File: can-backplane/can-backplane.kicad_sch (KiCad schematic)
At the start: 51 parts, among them J1 BATT, J10 DSUB-9, J11 DSUB-9, J12 Raspberry_Pi, J13 DSUB-9, J14 DSUB-9, J15 DSUB-9, J16 DSUB-9, J17 DSUB-9, J18 DSUB-9, J19 DSUB-9, J2 DSUB-9, J20 DSUB-9, J21 DSUB-9, J22 DSUB-9, J3 DSUB-9, J4 DSUB-9, J5 DSUB-9, J6 DSUB-9, J7 DSUB-9, J8 DSUB-9, J9 DSUB-9, U1 TPS566242DRLR, U2 TCAN1044VDDFR, U3 MCP2517FD-xJHA, Y1 40MHz

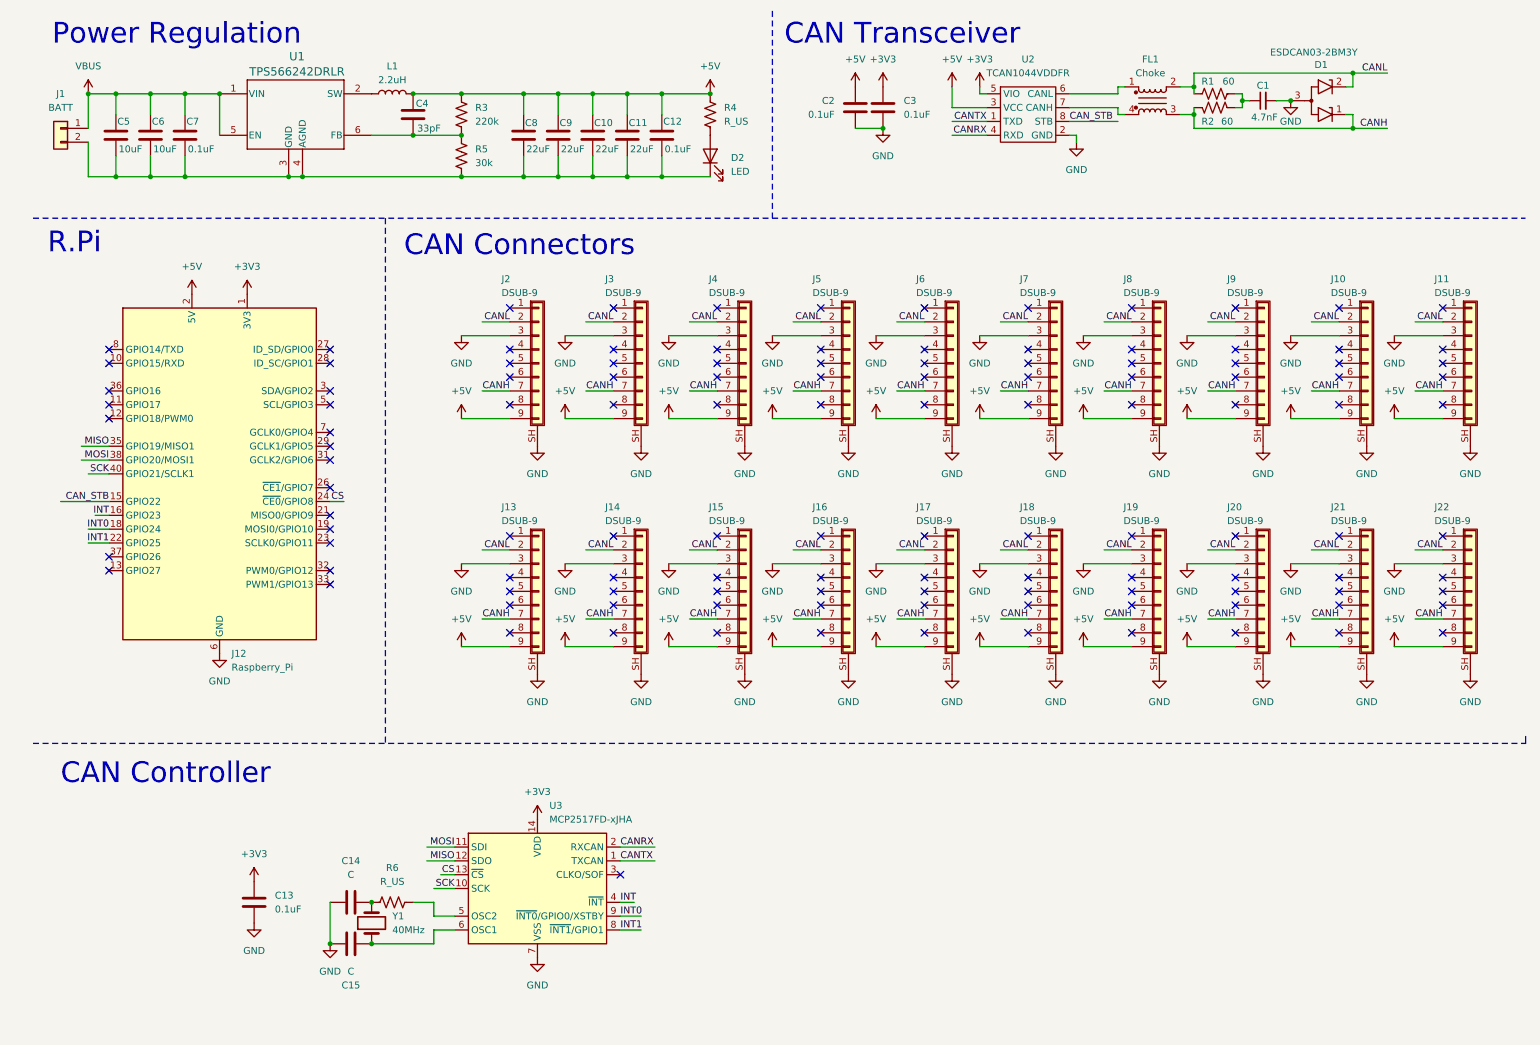
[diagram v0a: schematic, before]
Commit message: Added serial
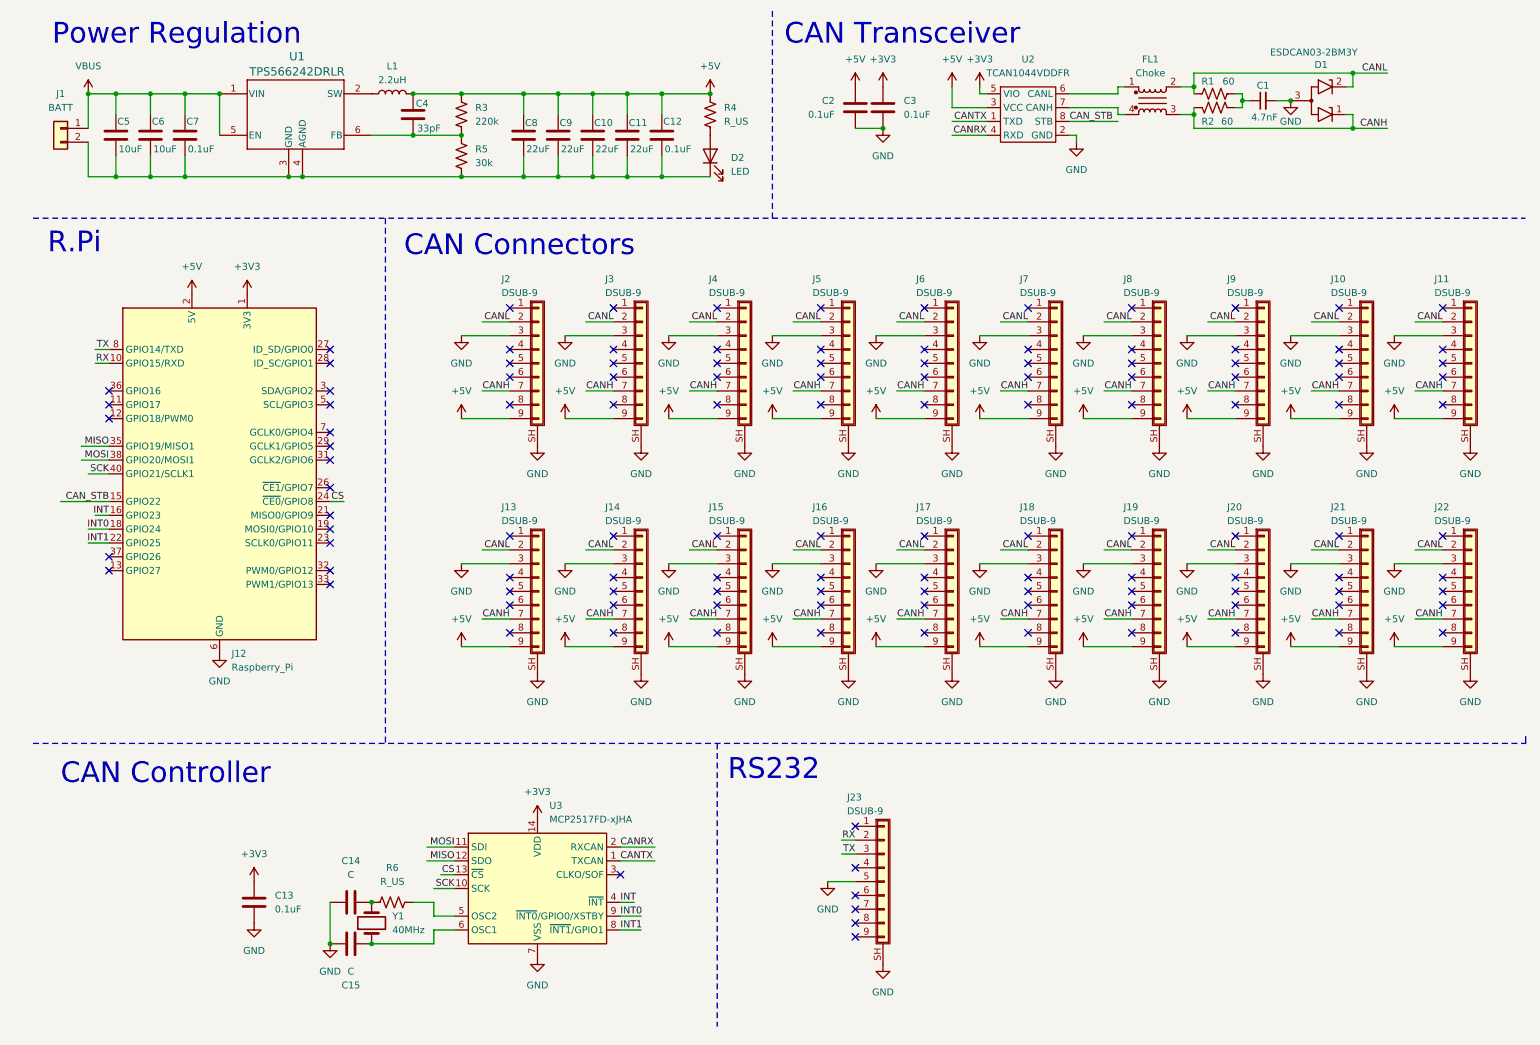
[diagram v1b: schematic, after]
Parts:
- added J23: DSUB-9, symbol Connector_Generic_Shielded:Conn_01x09_Shielded
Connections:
- net GND: now also J23.5 (Pin_5), J23.SH (Shield)
- net RX: now reaches J12.10 (GPIO15/RXD)
- net RX: now also J23.2 (Pin_2)
- net TX: now reaches J12.8 (GPIO14/TXD)
- net TX: now also J23.3 (Pin_3)
- no-connect marks 121 -> 125
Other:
- note added: "RS232"

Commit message: Added level shifting
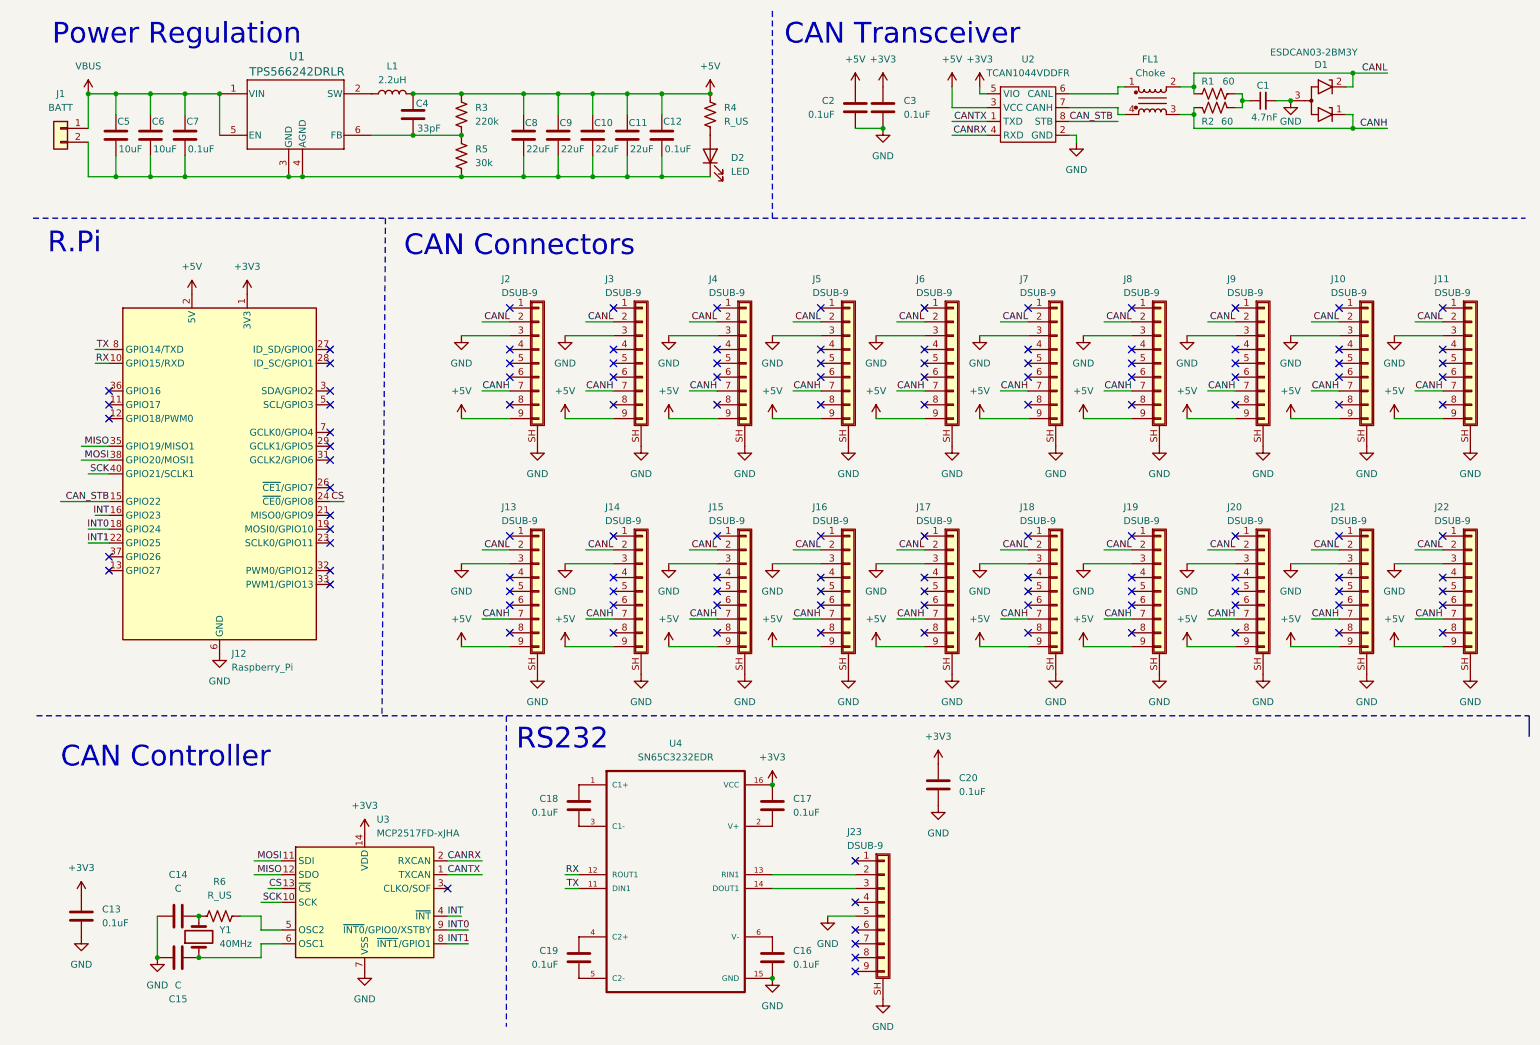
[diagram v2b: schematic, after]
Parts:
- added C16, C17, C18, C19, C20: 0.1uF, symbol Device:C
- added U4: SN65C3232EDR, SN65C3232EDR:SOIC127P600X175-16N, symbol Railspeeder:SN65C3232EDR
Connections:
- net +3V3: now also C17.1, C20.1, U4.16 (VCC)
- net GND: now also C16.2, C20.2, U4.15 (GND)
- net RX: now also U4.12 (ROUT1); no longer J23.2 (Pin_2)
- net TX: now also U4.11 (DIN1); no longer J23.3 (Pin_3)
- new net: C18.1, U4.1 (C1+)
- new net: C18.2, U4.3 (C1-)
- new net: C19.1, U4.4 (C2+)
- new net: C19.2, U4.5 (C2-)
- new net: J23.2 (Pin_2), U4.13 (RIN1)
- new net: J23.3 (Pin_3), U4.14 (DOUT1)
- new net: C17.2, U4.2 (V+)
- new net: C16.1, U4.6 (V-)
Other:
- moved on the sheet: C13, C14, C15, J23, R6, U3, Y1

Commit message: Component selection
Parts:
- C10, C11, C12, C16, C17, C18, C19, C20, C4, C5, C6, C7, C8, C9: footprint (none) -> Capacitor_SMD:C_0603_1608Metric
- C14, C15: value C -> CL; footprint (none) -> Capacitor_SMD:C_0603_1608Metric
- D2: value LED -> GREEN; footprint (none) -> LED_SMD:LED_0603_1608Metric
- J1: footprint (none) -> Connector_PinSocket_2.54mm:PinSocket_1x02_P2.54mm_Vertical
- J10, J11, J13, J14, J15, J16, J17, J18, J19, J2, J20, J21, J22, J23, J3, J4, J5, J6, J7, J8, J9: footprint (none) -> Connector_Dsub:DSUB-9_Female_Vertical_P2.77x2.84mm_MountingHoles
- J12: footprint (none) -> railspeeder:RPI_Hat_B+
- L1: footprint (none) -> Inductor_SMD_Wurth:L_Wurth_WE-LQSH-4020
- R3, R5: footprint (none) -> Resistor_SMD:R_0603_1608Metric
- R4: value R_US -> 220; footprint (none) -> Resistor_SMD:R_0603_1608Metric
- R6: value R_US -> REXT; footprint (none) -> Resistor_SMD:R_0603_1608Metric
- U1: footprint SOT5x3_DRL_TEX -> railspeeder:SOT5x3_DRL_TEX
- U4: footprint SN65C3232EDR:SOIC127P600X175-16N -> Package_SO:SOIC-16_3.9x9.9mm_P1.27mm
- Y1: footprint (none) -> Crystal:Crystal_SMD_Abracon_ABM10-4Pin_2.5x2.0mm

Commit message: PCB Work
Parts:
- added C21, C22: 4.7nF, Capacitor_SMD:C_0603_1608Metric, symbol Device:C_Small
- added R7: 5.1k, Resistor_SMD:R_0603_1608Metric, symbol Device:R_US
- J1: footprint Connector_PinSocket_2.54mm:PinSocket_1x02_P2.54mm_Vertical -> TerminalBlock_WAGO:TerminalBlock_WAGO_236-102_1x02_P5.00mm_45Degree
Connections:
- net +3V3: now also R7.2; no longer C17.1
- net CANH: now also C21.2
- net CANL: now also C22.2
- net CAN_STB: now also R7.1
- net GND: now also C17.2, C21.1, C22.1
- net at U4.2 (V+): now also C17.1; no longer C17.2
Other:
- moved on the sheet: C1, C17, D1

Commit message: PCB Work
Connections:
- net CANH: now also D1.2 (K2); no longer D1.1 (K1)
- net CANL: now also D1.1 (K1); no longer D1.2 (K2)
- net GND: now also C10.2, C11.2, C12.2, C5.2, C6.2, C7.2, C8.2, C9.2, D2.1 (K), J1.2 (Pin_2), R5.2, U1.3 (GND), U1.4 (AGND)
- net INT0: now also J12.22 (GPIO25); no longer J12.18 (GPIO24)
- net INT1: now also J12.18 (GPIO24); no longer J12.22 (GPIO25)
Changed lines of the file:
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@@
 	)
 	(junction
-		(at 254 27.94)
+		(at 135.89 41.91)
 		(diameter 0)
 		(color 0 0 0 0)
@@
 	)
 	(junction
+		(at 254 27.94)
+		(diameter 0)
+		(color 0 0 0 0)
+	)
+	(junction
 		(at 33.02 41.91)
 		(diameter 0)
@@
 	)
 	(label "INT0"
-		(at 25.4 106.68 180)
+		(at 25.4 109.22 180)
 		(fields_autoplaced yes)
 		(effects
@@
 	)
 	(label "INT1"
-		(at 25.4 109.22 180)
+		(at 25.4 106.68 180)
 		(fields_autoplaced yes)
 		(effects
@@
 	(symbol
 		(lib_id "power:GND")
+		(at 135.89 41.91 0)
+		(unit 1)
+		(exclude_from_sim no)
+		(in_bom yes)
+		(on_board yes)
+		(dnp no)
+		(fields_autoplaced yes)
+		(property "Reference" "#PWR086"
+			(at 135.89 48.26 0)
+			(effects
+				(font
+					(size 1.27 1.27)
+				)
+				(hide yes)
+			)
+		)
+		(property "Value" "GND"
+			(at 135.89 46.99 0)
+			(effects
+				(font
+					(size 1.27 1.27)
+				)
+			)
+		)
+		(property "Footprint" ""
+			(at 135.89 41.91 0)
+			(effects
+				(font
+					(size 1.27 1.27)
+				)
+				(hide yes)
+			)
+		)
+		(property "Datasheet" ""
+			(at 135.89 41.91 0)
+			(effects
+				(font
+					(size 1.27 1.27)
+				)
+				(hide yes)
+			)
+		)
+		(property "Description" "Power symbol creates a global label with name \"GND\" , ground"
+			(at 135.89 41.91 0)
+			(effects
+				(font
+					(size 1.27 1.27)
+				)
+				(hide yes)
+			)
+		)
+		(pin "1"
+		)
+		(instances
+			(project "can-backplane"
+				(path "/6aa1e968-9fc5-4472-b994-95c9fa68b877"
+					(reference "#PWR086")
+					(unit 1)
+				)
+			)
+		)
+	)
+	(symbol
+		(lib_id "power:GND")
 		(at 104.14 133.35 0)
 		(unit 1)
@@
 		(lib_id "Power_Protection:RCLAMP0582B")
 		(at 259.08 27.94 0)
-		(mirror x)
 		(unit 1)
 		(exclude_from_sim no)
@@
 		(dnp no)
 		(property "Reference" "D1"
-			(at 259.588 21.336 0)
+			(at 259.588 34.544 0)
 			(effects
 				(font
@@
 		)
 		(property "Value" "ESDCAN03-2BM3Y"
-			(at 258.2545 19.05 0)
+			(at 258.2545 36.83 0)
 			(effects
 				(font
@@
 		)
 		(property "Footprint" "Package_TO_SOT_SMD:SOT-416"
-			(at 259.08 20.32 0)
+			(at 259.08 35.56 0)
 			(effects
 				(font
@@
 		)
 		(property "Datasheet" "https://www.semtech.com/products/circuit-protection/low-capacitance/rclamp0582b"
-			(at 260.35 30.48 0)
+			(at 260.35 25.4 0)
 			(effects
 				(font

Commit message: Cut in  half
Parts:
- removed FL1: Choke, Inductor_SMD:L_CommonModeChoke_Coilcraft_0603USB, symbol Filter:Choke_Coilcraft_0603USB-142
- removed J1: BATT, TerminalBlock_WAGO:TerminalBlock_WAGO_236-102_1x02_P5.00mm_45Degree, symbol Connector_Generic:Conn_01x02
- removed J10, J11, J18, J19, J20, J21, J22, J7, J8, J9: DSUB-9, Connector_Dsub:DSUB-9_Female_Vertical_P2.77x2.84mm_MountingHoles, symbol Connector_Generic_Shielded:Conn_01x09_Shielded
- added FL1: DLW32SH510XF2L, DLW32PH_MUR, symbol Railspeeder:DLW32SH510XF2L
- added J3: 2601-1102, railspeeder:CONN2_2601-1102_WAG, symbol Railspeeder:2601-1102
- renumbered C2 to C1, C22 to C11, C16 to C12, C12 to C13, C8 to C14, C19 to C15, C4 to C16, C9 to C17, C5 to C18, C17 to C19, C14 to C2, C18 to C20, C6 to C21, C20 to C22, C13 to C4, C15 to C5, C1 to C6, C21 to C7, C11 to C8, C7 to C9, J12 to J1, J13 to J14, J14 to J15, J15 to J17, J17 to J18, J23 to J4, J3 to J5, J5 to J6, J4 to J7, J6 to J8, R7 to R1, R6 to R2, R5 to R3, R3 to R5, R1 to R6, R2 to R7, U2 to U1, U3 to U2, U1 to U3
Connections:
- net CANH: now also FL1.2
- net CANL: now also FL1.3
- net GND: now also J3.3 (2_1), J3.4 (2_2)
- net VBUS: now also J3.1 (1_1), J3.2 (1_2)
- net at U1.6 (CANL): now also FL1.4
- net at U1.7 (CANH): now also FL1.1
- no-connect marks 125 -> 75
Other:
- moved on the sheet: C1, C10, C11, C13, C14, C16, C17, C18, C21, C3, C6, C7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

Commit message: PCB work for final fab
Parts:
- C2: renamed from C5; value CL -> 6pF
- C4: renamed from C2; value CL -> 6pF
- FL1: footprint DLW32PH_MUR -> railspeeder:DLW32PH_MUR
- R2: value REXT -> 680
- renumbered C3 to C1, C14 to C10, C15 to C11, C16 to C12, C9 to C13, C17 to C14, C7 to C15, C10 to C16, C11 to C17, C21 to C20, C20 to C21, C4 to C3, C1 to C5, C8 to C6, C6 to C7, C12 to C8, C13 to C9, D2 to D1, D1 to D2, J15 to J10, J17 to J11, J16 to J12, J18 to J13, J4 to J2, J2 to J3, J3 to J4, J7 to J6, J6 to J7, J14 to J9, R6 to R5, R5 to R6, U4 to U3, U3 to U4
